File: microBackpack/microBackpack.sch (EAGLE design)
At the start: 54 parts, among them IC1 LM324D, IC2 LM324D, J2 USB_B_PTH, J4 2X6 FEMALE, U1 ATMEGA328P_TQFP, U2 5VREG-HS, U3 CP2102N-QFN24, U4 TVS_DIODE_4PK, U5 MCP4728, U6 78L09F

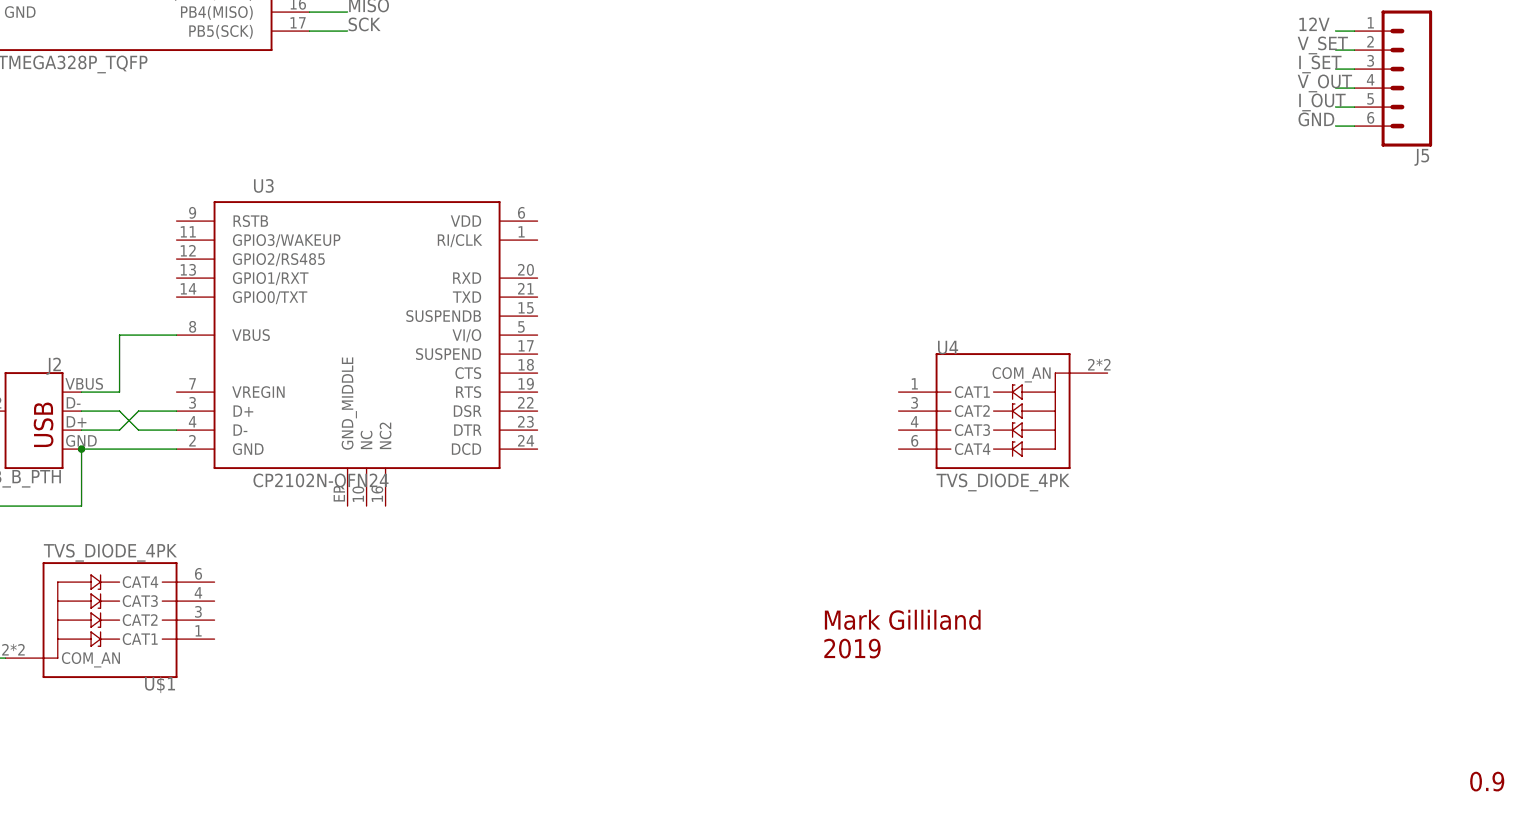
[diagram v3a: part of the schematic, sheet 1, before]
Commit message: Began board layout. Defined dimensions.
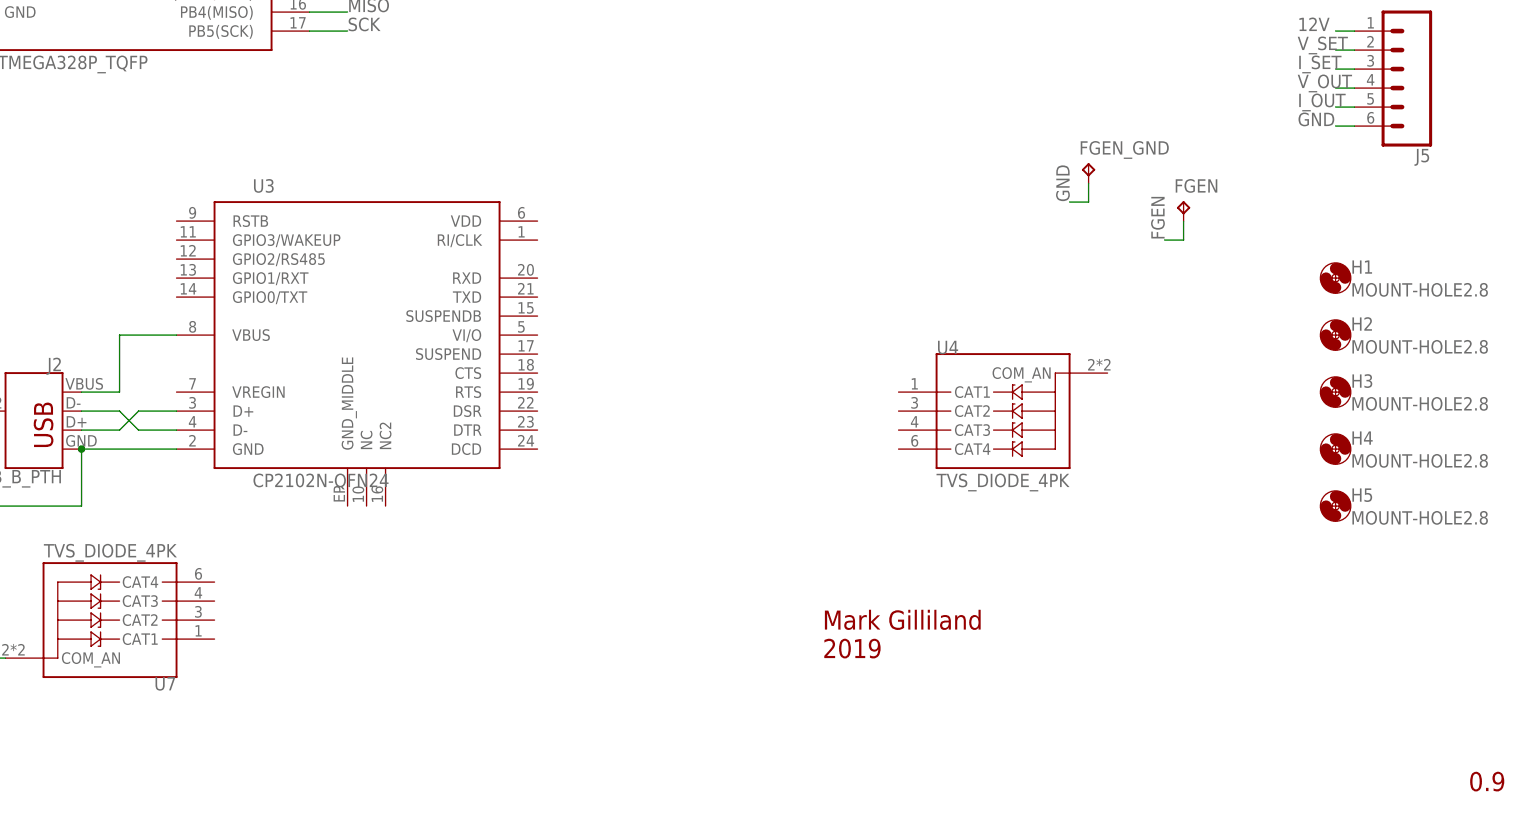
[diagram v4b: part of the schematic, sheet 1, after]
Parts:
- added FGEN, FGEN_GND: TPPAD1-20Y, testpad:TPPAD1-20Y
- added H1, H2, H3, H4, H5: MOUNT-HOLE2.8, holes:MOUNT-HOLE2.8
- renumbered U$1 to U7
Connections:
- net FGEN: now also FGEN.TP
- net GND: now also FGEN_GND.TP
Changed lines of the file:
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@@
 <part name="U2" library="microBackpackLib" deviceset="5VREG" device="-HS"/>
 <part name="U3" library="microBackpackLib" deviceset="CP2102N-QFN24" device=""/>
-<part name="U$1" library="microBackpackLib" deviceset="TVS_DIODE_4PK" device=""/>
+<part name="U7" library="microBackpackLib" deviceset="TVS_DIODE_4PK" device=""/>
 <part name="J1" library="SparkFun-Connectors" library_urn="urn:adsk.eagle:library:513" deviceset="CONN_03X2" device="2X3_SILK_MALE_PTH" package3d_urn="urn:adsk.eagle:package:38016/1"/>
 <part name="P+1" library="supply1" library_urn="urn:adsk.eagle:library:371" deviceset="VCC" device=""/>
@@
 <part name="R28" library="rcl" library_urn="urn:adsk.eagle:library:334" deviceset="R-US_" device="R0805" package3d_urn="urn:adsk.eagle:package:23553/2" value="10k"/>
 <part name="GND19" library="supply1" library_urn="urn:adsk.eagle:library:371" deviceset="GND" device=""/>
+<part name="H1" library="holes" library_urn="urn:adsk.eagle:library:237" deviceset="MOUNT-HOLE" device="2.8" package3d_urn="urn:adsk.eagle:package:14271/1"/>
+<part name="H2" library="holes" library_urn="urn:adsk.eagle:library:237" deviceset="MOUNT-HOLE" device="2.8" package3d_urn="urn:adsk.eagle:package:14271/1"/>
+<part name="H3" library="holes" library_urn="urn:adsk.eagle:library:237" deviceset="MOUNT-HOLE" device="2.8" package3d_urn="urn:adsk.eagle:package:14271/1"/>
+<part name="H4" library="holes" library_urn="urn:adsk.eagle:library:237" deviceset="MOUNT-HOLE" device="2.8" package3d_urn="urn:adsk.eagle:package:14271/1"/>
+<part name="FGEN" library="testpad" library_urn="urn:adsk.eagle:library:385" deviceset="TP" device="PAD1-20Y" package3d_urn="urn:adsk.eagle:package:27951/1"/>
+<part name="H5" library="holes" library_urn="urn:adsk.eagle:library:237" deviceset="MOUNT-HOLE" device="2.8" package3d_urn="urn:adsk.eagle:package:14271/1"/>
+<part name="FGEN_GND" library="testpad" library_urn="urn:adsk.eagle:library:385" deviceset="TP" device="PAD1-20Y" package3d_urn="urn:adsk.eagle:package:27951/1"/>
 </parts>
 <sheets>
@@
 <attribute name="VALUE" x="101.6" y="48.26" size="1.778" layer="96"/>
 </instance>
-<instance part="U$1" gate="G$1" x="78.74" y="30.48" smashed="yes" rot="R180">
+<instance part="U7" gate="G$1" x="78.74" y="30.48" smashed="yes" rot="R180">
 <attribute name="NAME" x="91.44" y="22.86" size="1.778" layer="95" rot="R180"/>
 <attribute name="VALUE" x="91.44" y="40.64" size="1.778" layer="96" rot="R180"/>
@@
 <instance part="GND17" gate="1" x="12.7" y="181.61" smashed="yes">
 <attribute name="VALUE" x="10.16" y="179.07" size="1.778" layer="96"/>
+</instance>
+<instance part="H1" gate="G$1" x="246.38" y="76.2" smashed="yes">
+<attribute name="NAME" x="248.412" y="76.7842" size="1.778" layer="95"/>
+<attribute name="VALUE" x="248.412" y="73.7362" size="1.778" layer="96"/>
+</instance>
+<instance part="H2" gate="G$1" x="246.38" y="68.58" smashed="yes">
+<attribute name="NAME" x="248.412" y="69.1642" size="1.778" layer="95"/>
+<attribute name="VALUE" x="248.412" y="66.1162" size="1.778" layer="96"/>
+</instance>
+<instance part="H3" gate="G$1" x="246.38" y="60.96" smashed="yes">
+<attribute name="NAME" x="248.412" y="61.5442" size="1.778" layer="95"/>
+<attribute name="VALUE" x="248.412" y="58.4962" size="1.778" layer="96"/>
+</instance>
+<instance part="H4" gate="G$1" x="246.38" y="53.34" smashed="yes">
+<attribute name="NAME" x="248.412" y="53.9242" size="1.778" layer="95"/>
+<attribute name="VALUE" x="248.412" y="50.8762" size="1.778" layer="96"/>
+</instance>
+<instance part="FGEN" gate="G$1" x="226.06" y="86.36" smashed="yes">
+<attribute name="NAME" x="224.79" y="87.63" size="1.778" layer="95"/>
+<attribute name="TP_SIGNAL_NAME" x="227.33" y="85.09" size="1.778" layer="97"/>
+</instance>
+<instance part="H5" gate="G$1" x="246.38" y="45.72" smashed="yes">
+<attribute name="NAME" x="248.412" y="46.3042" size="1.778" layer="95"/>
+<attribute name="VALUE" x="248.412" y="43.2562" size="1.778" layer="96"/>
+</instance>
+<instance part="FGEN_GND" gate="G$1" x="213.36" y="91.44" smashed="yes">
+<attribute name="NAME" x="212.09" y="92.71" size="1.778" layer="95"/>
+<attribute name="TP_SIGNAL_NAME" x="214.63" y="90.17" size="1.778" layer="97"/>
 </instance>
 </instances>
@@
 <pinref part="GND17" gate="1" pin="GND"/>
 </segment>
+<segment>
+<pinref part="FGEN_GND" gate="G$1" pin="TP"/>
+<wire x1="213.36" y1="88.9" x2="213.36" y2="86.36" width="0.1524" layer="91"/>
+<wire x1="213.36" y1="86.36" x2="210.82" y2="86.36" width="0.1524" layer="91"/>
+<label x="210.82" y="86.36" size="1.778" layer="95" rot="R90"/>
+</segment>
 </net>
 <net name="MISO" class="0">
@@
 <pinref part="J2" gate="G$1" pin="SHIELD"/>
 <wire x1="66.04" y1="58.42" x2="66.04" y2="45.72" width="0.1524" layer="91"/>
-<pinref part="U$1" gate="G$1" pin="COM_AN"/>
+<pinref part="U7" gate="G$1" pin="COM_AN"/>
 <wire x1="66.04" y1="45.72" x2="66.04" y2="25.4" width="0.1524" layer="91"/>
 <wire x1="66.04" y1="25.4" x2="68.58" y2="25.4" width="0.1524" layer="91"/>
@@
 </segment>
 </net>
+<net name="FGEN" class="0">
+<segment>
+<pinref part="FGEN" gate="G$1" pin="TP"/>
+<wire x1="226.06" y1="83.82" x2="226.06" y2="81.28" width="0.1524" layer="91"/>
+<wire x1="226.06" y1="81.28" x2="223.52" y2="81.28" width="0.1524" layer="91"/>
+<label x="223.52" y="81.28" size="1.778" layer="95" rot="R90"/>
+</segment>
+</net>

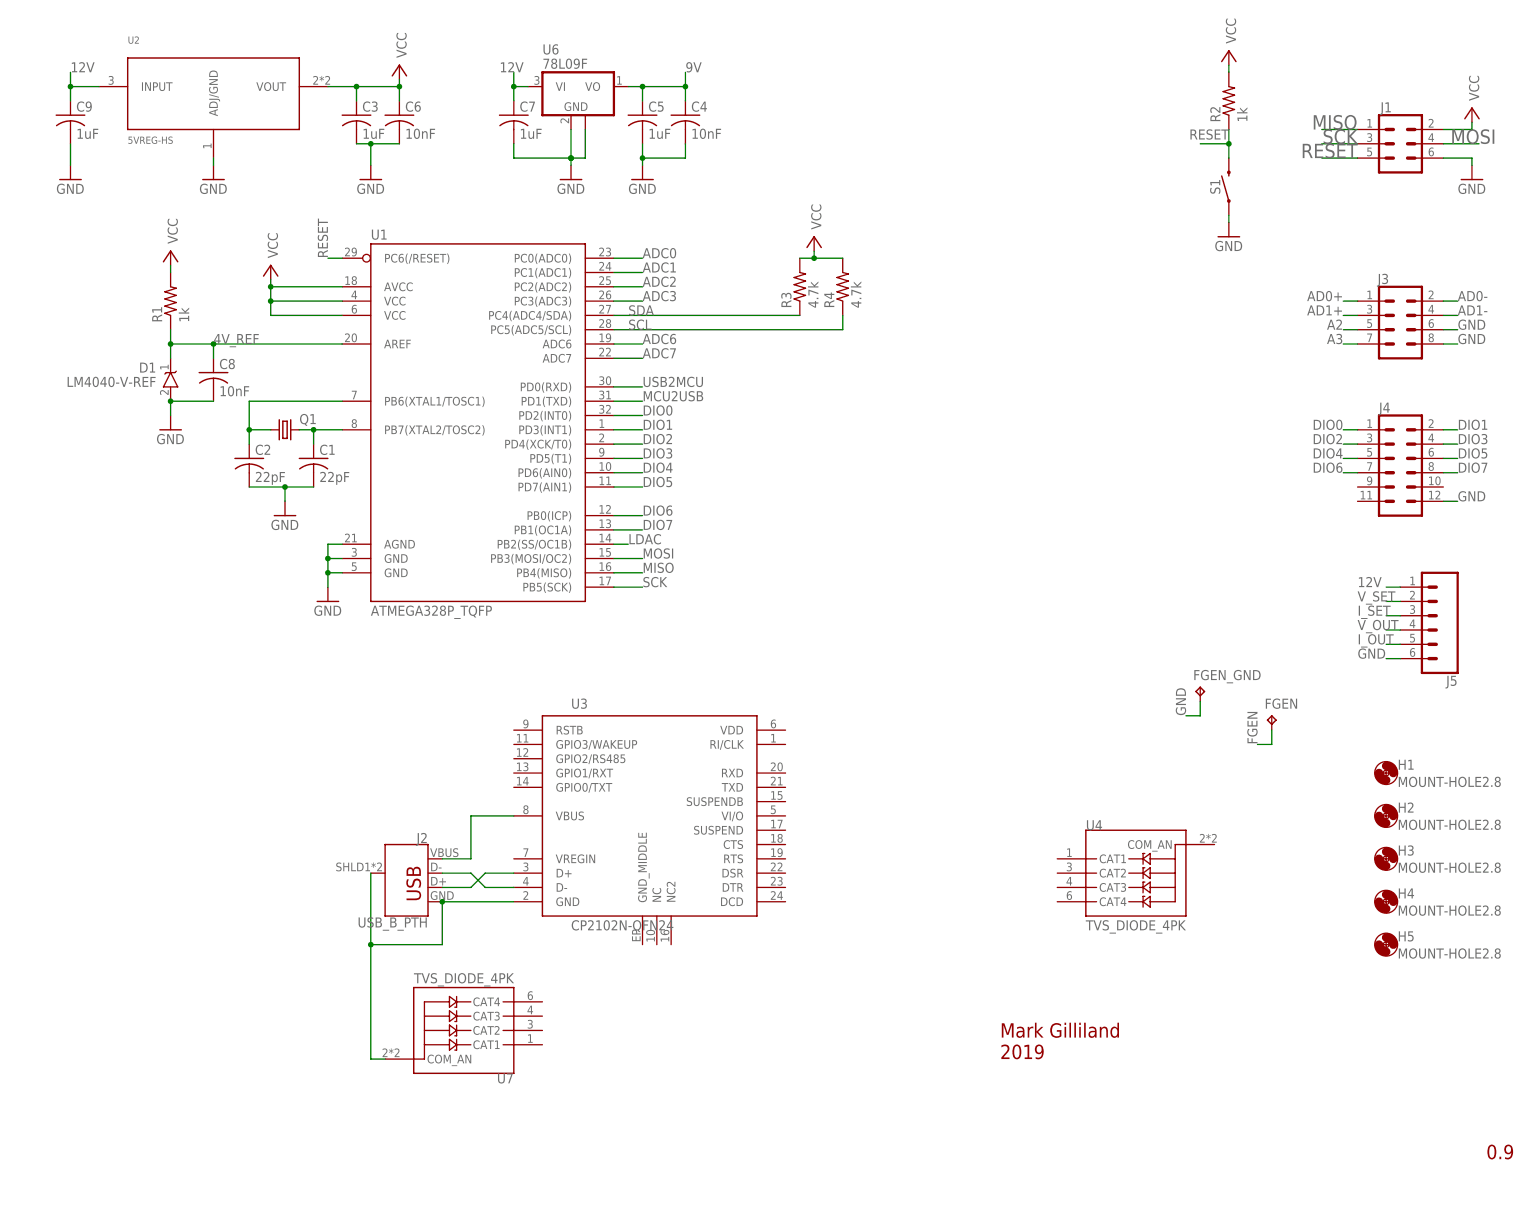
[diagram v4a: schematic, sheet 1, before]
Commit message: Spec'd header part. Added DIO protection diodes and resistors. Significantly more routing done
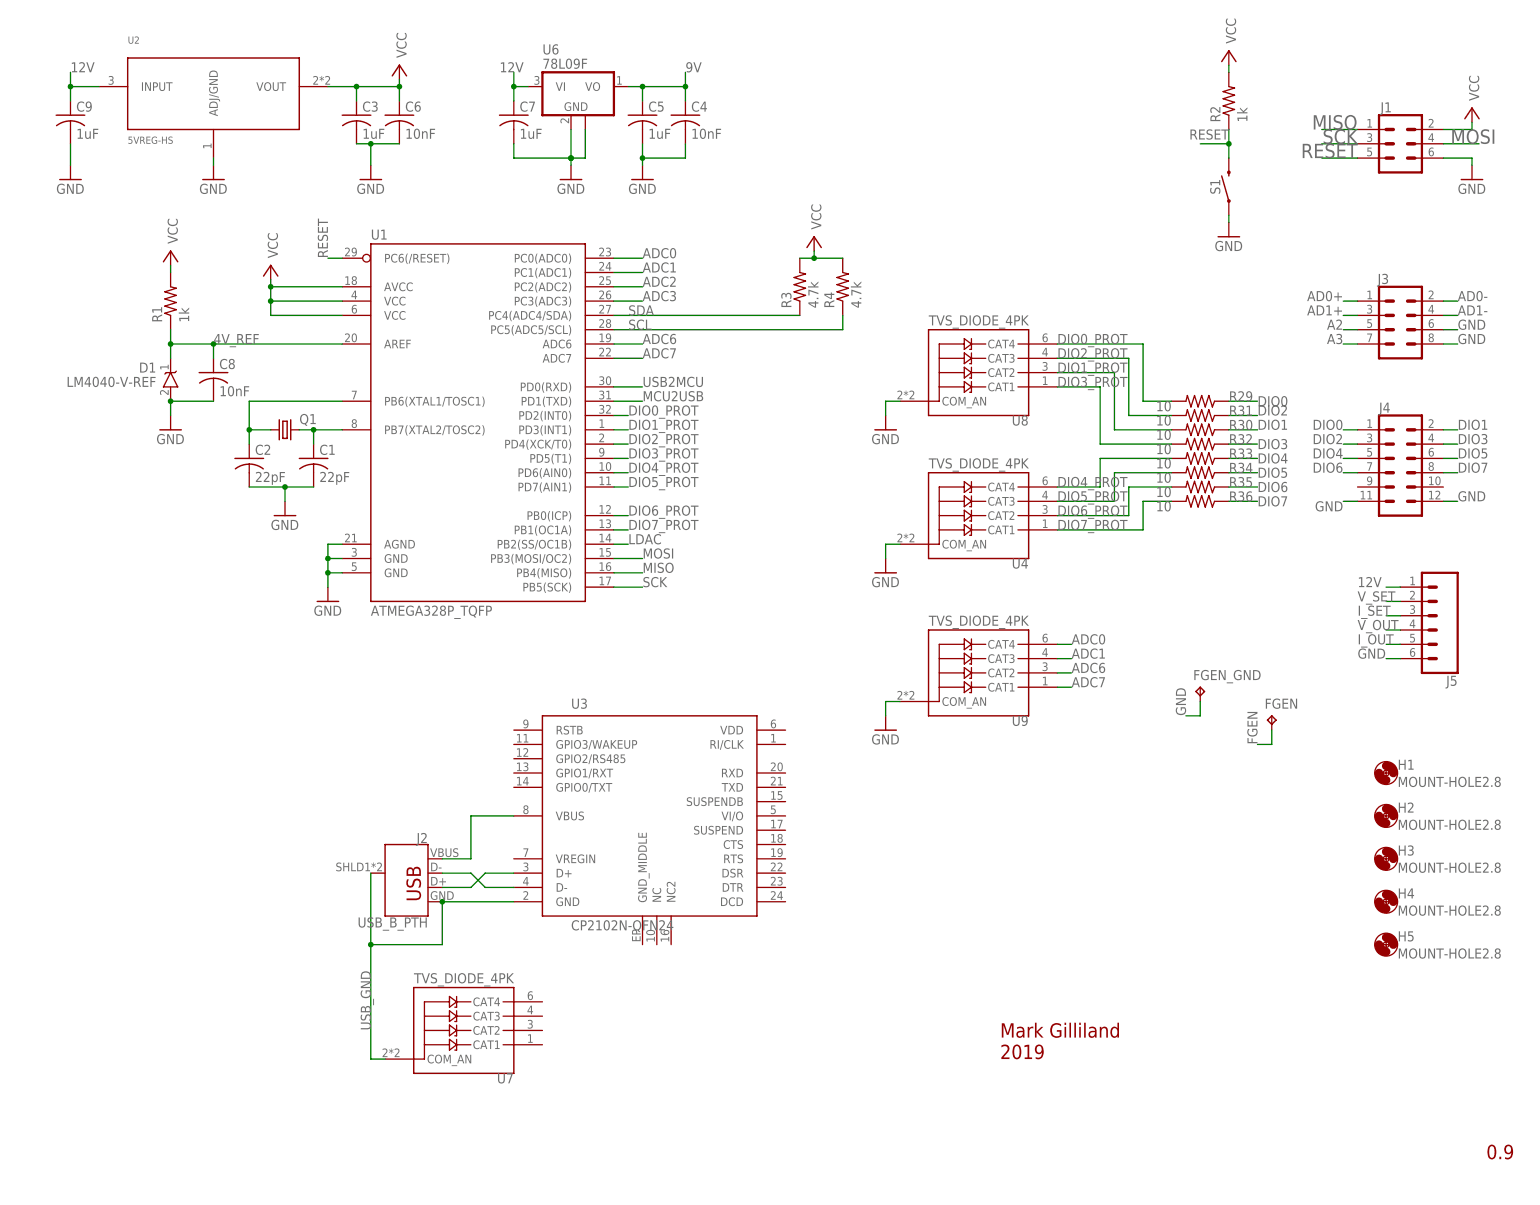
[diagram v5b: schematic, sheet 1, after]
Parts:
- added R29, R30, R31, R32, R33, R34, R35, R36: 10, rcl:R-US_R0805
- added U8, U9: TVS_DIODE_4PK, microBackpackLib:TVS_DIODE_4PK
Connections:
- net N$4 renamed USB_GND
- new net DIO0_PROT: R29.2, U1.PD2(INT0), U8.CAT4
- new net DIO1_PROT: R30.2, U1.PD3(INT1), U8.CAT2
- new net DIO2_PROT: R31.2, U1.PD4(XCK/T0), U8.CAT3
- new net DIO3_PROT: R32.2, U1.PD5(T1), U8.CAT1
- new net DIO4_PROT: R33.2, U1.PD6(AIN0), U4.CAT4
- new net DIO5_PROT: R34.2, U1.PD7(AIN1), U4.CAT3
- new net DIO6_PROT: R35.2, U1.PB0(ICP), U4.CAT2
- new net DIO7_PROT: R36.2, U1.PB1(OC1A), U4.CAT1
- net ADC0: now also U9.CAT4
- net ADC1: now also U9.CAT3
- net ADC6: now also U9.CAT2
- net ADC7: now also U9.CAT1
- net DIO0: now also R29.1; no longer U1.PD2(INT0)
- net DIO1: now also R30.1; no longer U1.PD3(INT1)
- net DIO2: now also R31.1; no longer U1.PD4(XCK/T0)
- net DIO3: now also R32.1; no longer U1.PD5(T1)
- net DIO4: now also R33.1; no longer U1.PD6(AIN0)
- net DIO5: now also R34.1; no longer U1.PD7(AIN1)
- net DIO6: now also R35.1; no longer U1.PB0(ICP)
- net DIO7: now also R36.1; no longer U1.PB1(OC1A)
- net GND: now also J4.11, U4.COM_AN, U8.COM_AN, U9.COM_AN
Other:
- moved on the sheet: U4
